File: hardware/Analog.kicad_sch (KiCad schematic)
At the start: 82 parts, among them J1 PH2-04-UA, J10 PH1-03-UA, J11 PH1-03-UA, J12 PH1-03-UA, J2 PH2-04-UA, J3 PH2-04-UA, J4 PH2-04-UA, J5 PH2-04-UA, J6 PH2-04-UA, J7 PH1-03-UA, J8 PH1-03-UA, J9 PH1-03-UA, U11 INA2128UA_1K, U12 INA2128UA_1K, U13 INA2128UA_1K, U14 TLC274AIDR, U15 TLC274AIDR, U16 TLC274AIDR, U17 TL431LIBQDBZRQ1

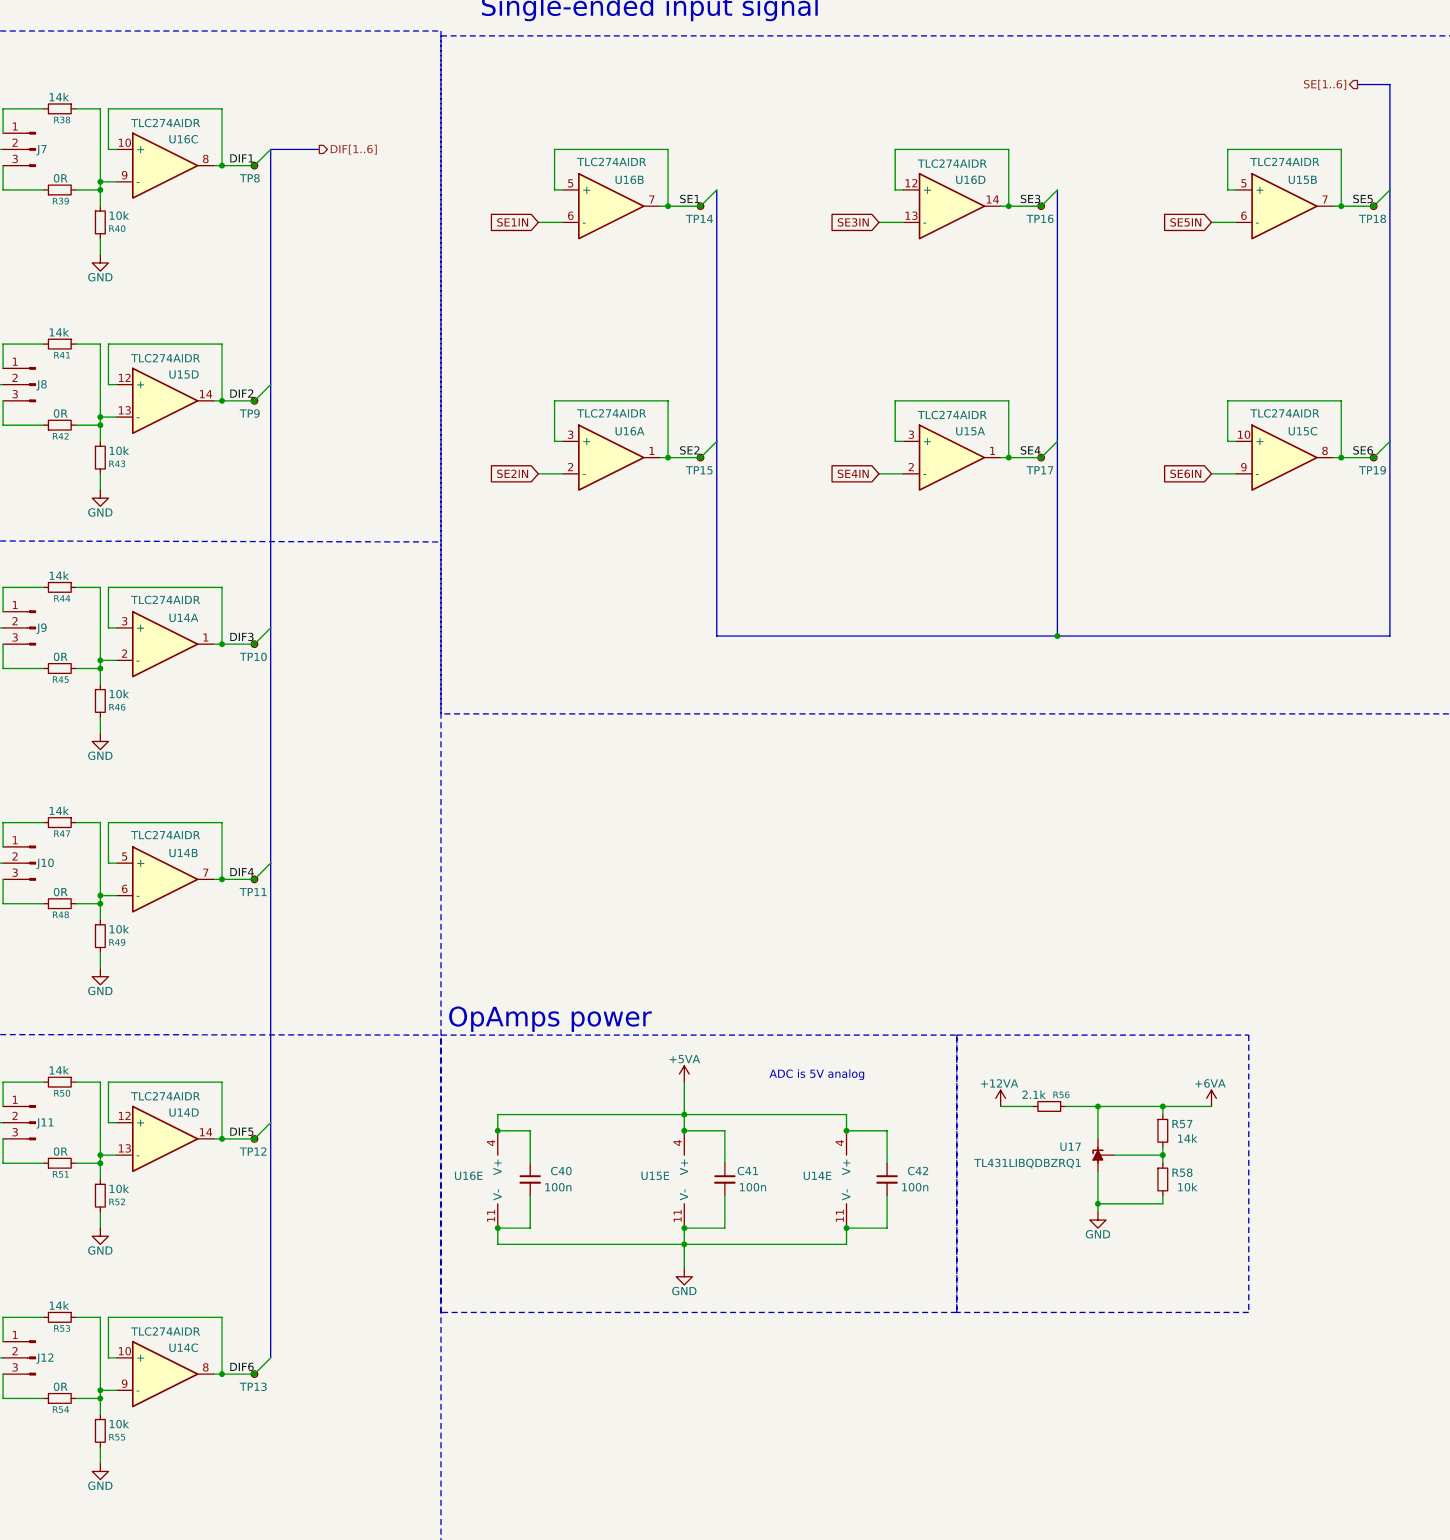
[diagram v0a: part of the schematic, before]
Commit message: Fixed pinout errors & changed branch name
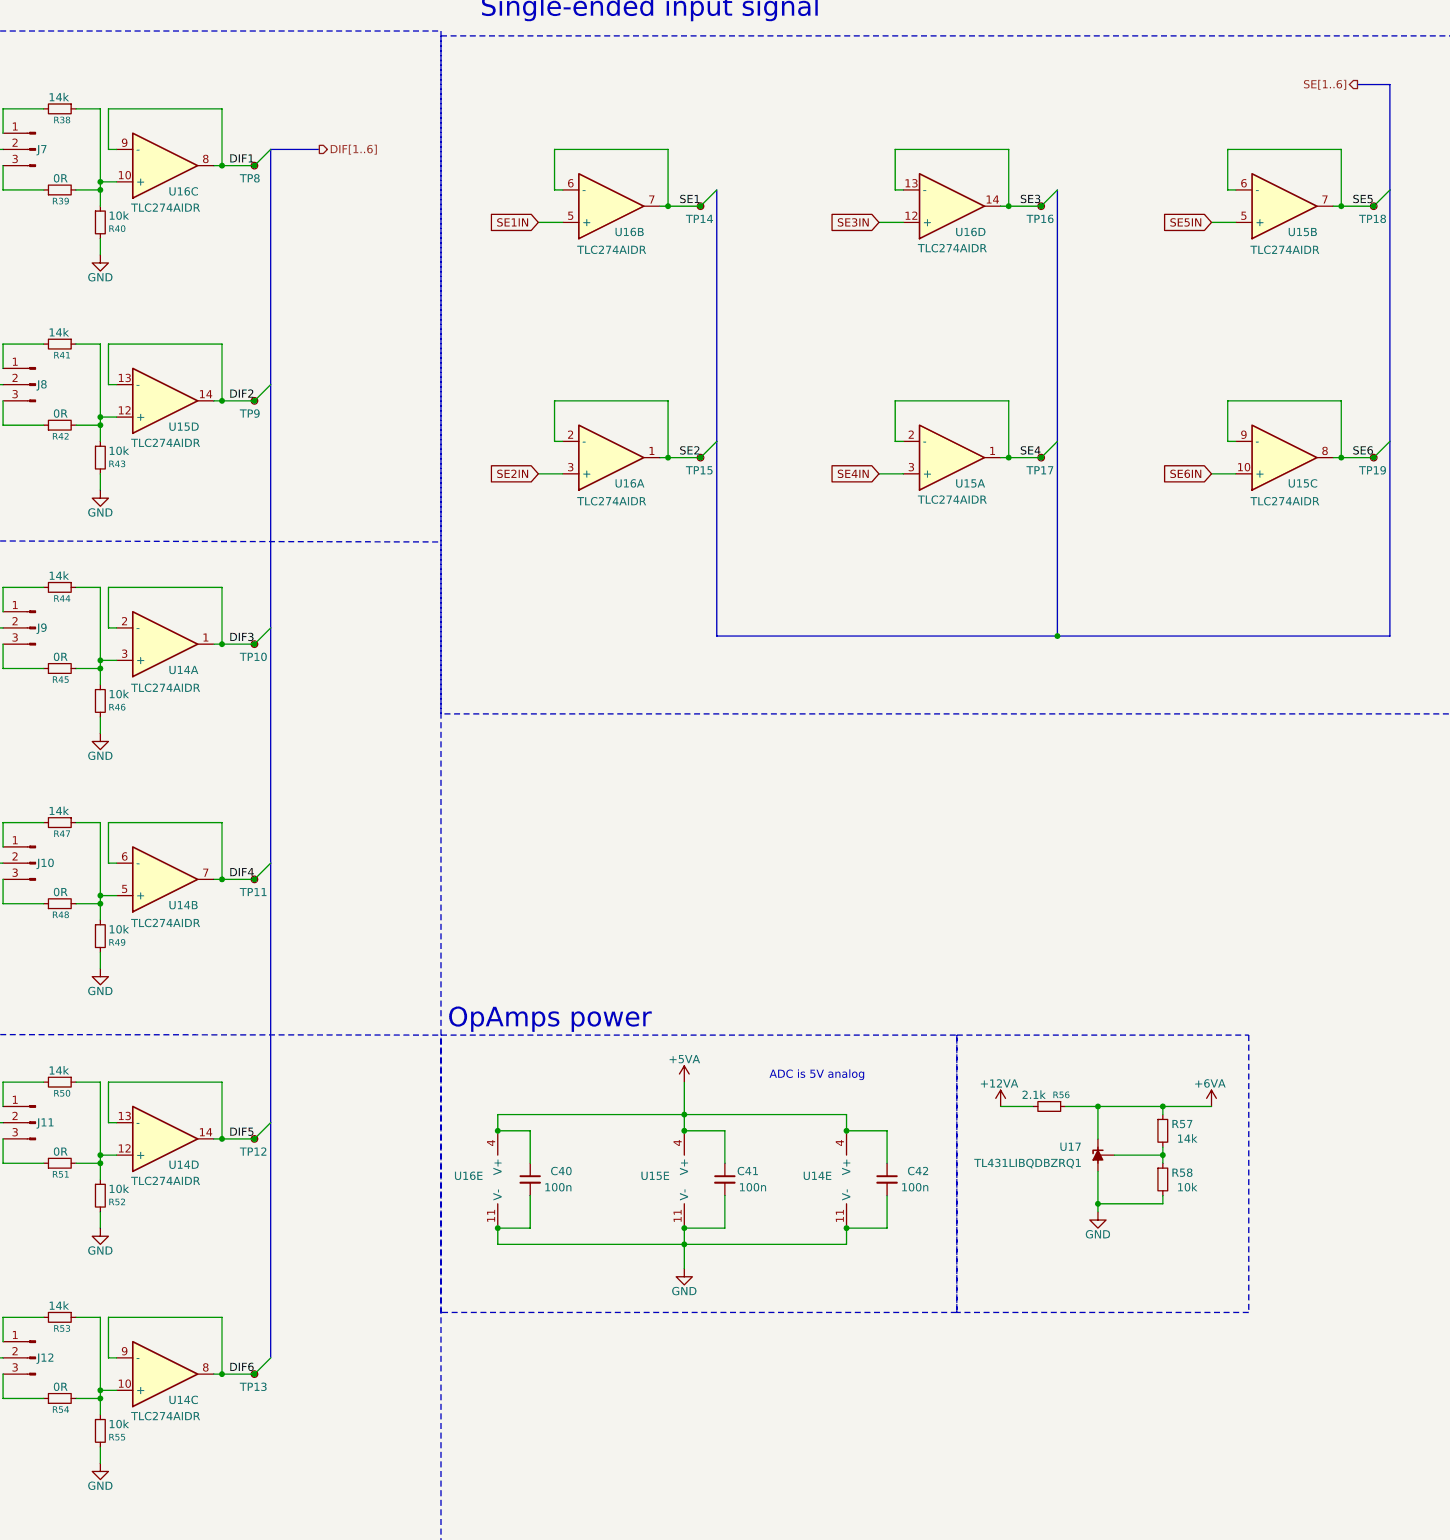
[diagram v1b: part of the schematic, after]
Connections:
- net DIF1: now also U16.9 (-); no longer U16.10 (+)
- net DIF2: now also U15.13 (-); no longer U15.12 (+)
- net DIF3: now also U14.2 (-); no longer U14.3 (+)
- net DIF4: now also U14.6 (-); no longer U14.5 (+)
- net DIF5: now also U14.13 (-); no longer U14.12 (+)
- net DIF6: now also U14.9 (-); no longer U14.10 (+)
- net SE1: now also U16.6 (-); no longer U16.5 (+)
- net SE1IN: now also U16.5 (+); no longer U16.6 (-)
- net SE2: now also U16.2 (-); no longer U16.3 (+)
- net SE2IN: now also U16.3 (+); no longer U16.2 (-)
- net SE3: now also U16.13 (-); no longer U16.12 (+)
- net SE3IN: now also U16.12 (+); no longer U16.13 (-)
- net SE4: now also U15.2 (-); no longer U15.3 (+)
- net SE4IN: now also U15.3 (+); no longer U15.2 (-)
- net SE5: now also U15.6 (-); no longer U15.5 (+)
- net SE5IN: now also U15.5 (+); no longer U15.6 (-)
- net SE6: now also U15.9 (-); no longer U15.10 (+)
- net SE6IN: now also U15.10 (+); no longer U15.9 (-)
- net at R47.1, R48.2, R49.1: now also U14.5 (+); no longer U14.6 (-)
- net at R53.1, R54.2, R55.1: now also U14.10 (+); no longer U14.9 (-)
- net at R41.1, R42.2, R43.1: now also U15.12 (+); no longer U15.13 (-)
- net at R44.1, R45.2, R46.1: now also U14.3 (+); no longer U14.2 (-)
- net at R38.1, R39.2, R40.1: now also U16.10 (+); no longer U16.9 (-)
- net at R50.1, R51.2, R52.1: now also U14.12 (+); no longer U14.13 (-)
